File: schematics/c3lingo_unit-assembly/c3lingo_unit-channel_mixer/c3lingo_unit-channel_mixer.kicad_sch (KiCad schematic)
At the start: 93 parts, among them J301 Interconnect, J303 I/O, Q301 MMBFJ113, SW301 OnAir_X, SW302 Mute_X, U301 TL072, U302 LM339, U303 LM339, U304 LM339, U305 LM833-N

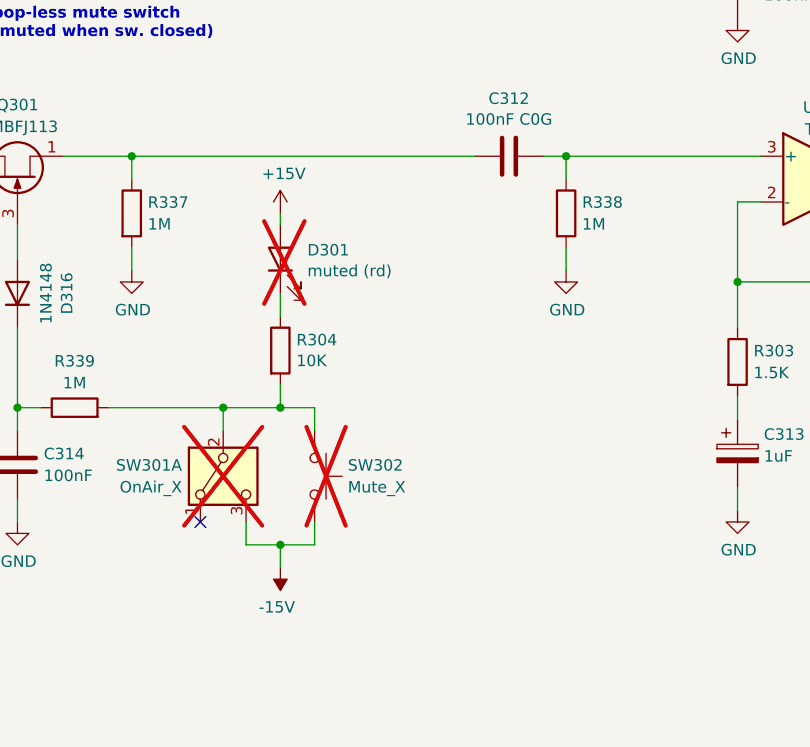
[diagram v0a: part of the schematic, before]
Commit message: Channel-Mixer: Invert mute LED logic (to be an on-air LED)
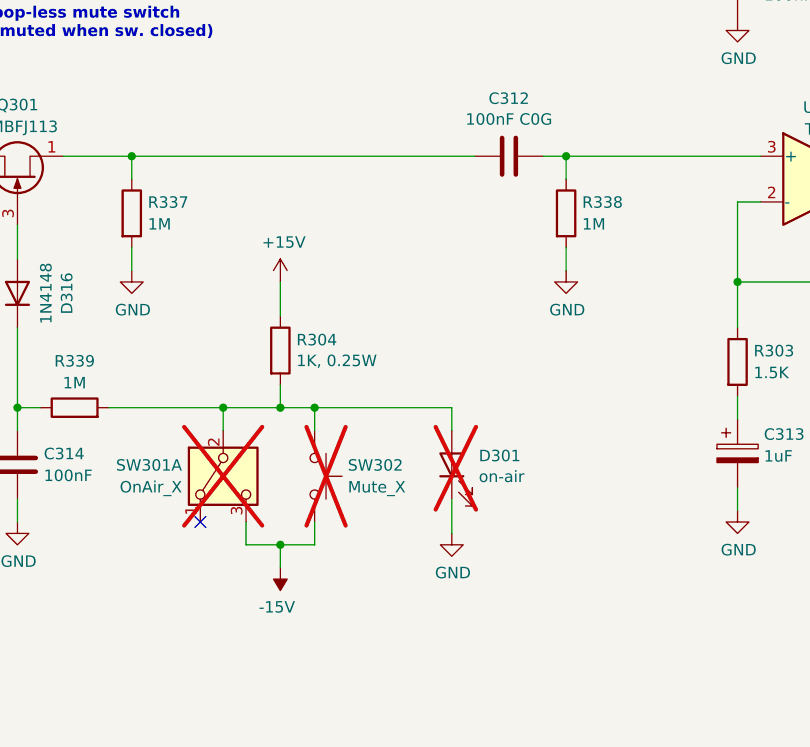
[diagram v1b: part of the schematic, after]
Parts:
- D301: value muted (rd) -> on-air
- R304: value 10K -> 1K, 0.25W; footprint Resistor_SMD:R_0805_2012Metric_Pad1.20x1.40mm_HandSolder -> Resistor_SMD:R_1206_3216Metric_Pad1.30x1.75mm_HandSolder; LCSC Part # C17414 -> C4410
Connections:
- net +15V: now also R304.1; no longer D301.2 (A)
- net GND: now also D301.1 (K)
- net at R304.2, R339.2, SW301.2 (B)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: now also D301.2 (A)
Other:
- moved on the sheet: D301
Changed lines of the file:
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@@
 	)
 	(junction
+		(at 99.06 91.44)
+		(diameter 0)
+		(color 0 0 0 0)
+	)
+	(junction
 		(at 304.8 149.86)
 		(diameter 0)
@@
 	(wire
 		(pts
-			(xy 95.25 78.74) (xy 95.25 81.28)
-		)
-		(stroke
-			(width 0)
-			(type default)
-		)
-	)
-	(wire
-		(pts
 			(xy 229.87 261.62) (xy 229.87 266.7)
 		)
@@
 	(wire
 		(pts
+			(xy 95.25 77.47) (xy 95.25 81.28)
+		)
+		(stroke
+			(width 0)
+			(type default)
+		)
+	)
+	(wire
+		(pts
 			(xy 85.09 213.36) (xy 85.09 215.9)
 		)
@@
 	(wire
 		(pts
-			(xy 95.25 69.85) (xy 95.25 71.12)
-		)
-		(stroke
-			(width 0)
-			(type default)
-		)
-	)
-	(wire
-		(pts
 			(xy 166.37 66.04) (xy 163.83 66.04)
 		)
@@
 	(wire
 		(pts
+			(xy 114.3 91.44) (xy 99.06 91.44)
+		)
+		(stroke
+			(width 0)
+			(type default)
+		)
+	)
+	(wire
+		(pts
 			(xy 304.8 170.18) (xy 304.8 172.72)
 		)
@@
 	(wire
 		(pts
+			(xy 114.3 93.98) (xy 114.3 91.44)
+		)
+		(stroke
+			(width 0)
+			(type default)
+		)
+	)
+	(wire
+		(pts
 			(xy 127 63.5) (xy 148.59 63.5)
 		)
@@
 	(wire
 		(pts
+			(xy 114.3 101.6) (xy 114.3 105.41)
+		)
+		(stroke
+			(width 0)
+			(type default)
+		)
+	)
+	(wire
+		(pts
 			(xy 69.85 215.9) (xy 69.85 218.44)
 		)
@@
 	(symbol
 		(lib_id "Device:LED")
-		(at 95.25 74.93 90)
+		(at 114.3 97.79 90)
 		(unit 1)
 		(exclude_from_sim no)
@@
 		(dnp yes)
 		(property "Reference" "D301"
-			(at 98.2472 73.9394 90)
+			(at 117.2972 96.7994 90)
 			(effects
 				(font
@@
 			)
 		)
-		(property "Value" "muted (rd)"
-			(at 98.2472 76.2508 90)
+		(property "Value" "on-air"
+			(at 117.2972 99.1108 90)
 			(effects
 				(font
@@
 		)
 		(property "Footprint" "LED_THT:LED_D3.0mm"
-			(at 95.25 74.93 0)
+			(at 114.3 97.79 0)
 			(effects
 				(font
@@
 		)
 		(property "Datasheet" "~"
-			(at 95.25 74.93 0)
+			(at 114.3 97.79 0)
 			(effects
 				(font
@@
 		)
 		(property "Description" "Light emitting diode"
-			(at 95.25 74.93 0)
+			(at 114.3 97.79 0)
 			(effects
 				(font
@@
 		)
 		(property "Model" "Kingbright WP710A10LID"
-			(at 95.25 74.93 0)
+			(at 114.3 97.79 0)
 			(effects
 				(font
@@
 		)
 		(property "LCSC Part #" ""
-			(at 95.25 74.93 0)
+			(at 114.3 97.79 0)
 			(effects
 				(font
@@
 		)
 		(property "FT Rotation Offset" ""
-			(at 95.25 74.93 0)
+			(at 114.3 97.79 0)
 			(effects
 				(font
@@
 		)
 		(property "Sim.Pins" "1=K 2=A"
-			(at 95.25 74.93 0)
+			(at 114.3 97.79 0)
 			(effects
 				(font
@@
 			)
 		)
-		(property "Value" "10K"
+		(property "Value" "1K, 0.25W"
 			(at 97.028 86.233 0)
 			(effects
@@
 			)
 		)
-		(property "Footprint" "Resistor_SMD:R_0805_2012Metric_Pad1.20x1.40mm_HandSolder"
+		(property "Footprint" "Resistor_SMD:R_1206_3216Metric_Pad1.30x1.75mm_HandSolder"
 			(at 93.472 85.09 90)
 			(effects
@@
 			)
 		)
-		(property "LCSC Part #" "C17414"
+		(property "LCSC Part #" "C4410"
 			(at 95.25 85.09 0)
 			(effects
@@
 	(symbol
 		(lib_id "power:+15V")
-		(at 95.25 69.85 0)
+		(at 95.25 77.47 0)
 		(unit 1)
 		(exclude_from_sim no)
@@
 		(dnp no)
 		(property "Reference" "#PWR0301"
-			(at 95.25 73.66 0)
+			(at 95.25 81.28 0)
 			(effects
 				(font
@@
 		)
 		(property "Value" "+15V"
-			(at 95.631 65.4558 0)
+			(at 95.631 73.0758 0)
 			(effects
 				(font
@@
 		)
 		(property "Footprint" ""
-			(at 95.25 69.85 0)
+			(at 95.25 77.47 0)
 			(effects
 				(font
@@
 		)
 		(property "Datasheet" ""
-			(at 95.25 69.85 0)
+			(at 95.25 77.47 0)
 			(effects
 				(font
@@
 		)
 		(property "Description" "Power symbol creates a global label with name \"+15V\""
-			(at 95.25 69.85 0)
+			(at 95.25 77.47 0)
 			(effects
 				(font
@@
 					(unit 1)
 				)
+			)
+		)
+	)
+	(symbol
+		(lib_id "power:GND")
+		(at 114.3 105.41 0)
+		(unit 1)
+		(exclude_from_sim no)
+		(in_bom yes)
+		(on_board yes)
+		(dnp no)
+		(property "Reference" "#PWR0333"
+			(at 114.3 111.76 0)
+			(effects
+				(font
+					(size 1.27 1.27)
+				)
+				(hide yes)
+			)
+		)
+		(property "Value" "GND"
+			(at 114.427 109.8042 0)
+			(effects
+				(font
+					(size 1.27 1.27)
+				)
+			)
+		)
+		(property "Footprint" ""
+			(at 114.3 105.41 0)
+			(effects
+				(font
+					(size 1.27 1.27)
+				)
+				(hide yes)
+			)
+		)
+		(property "Datasheet" ""
+			(at 114.3 105.41 0)
+			(effects
+				(font
+					(size 1.27 1.27)
+				)
+				(hide yes)
+			)
+		)
+		(property "Description" "Power symbol creates a global label with name \"GND\" , ground"
+			(at 114.3 105.41 0)
+			(effects
+				(font
+					(size 1.27 1.27)
+				)
+				(hide yes)
+			)
+		)
+		(pin "1"
+		)
+		(instances
+			(project "c3lingo_unit-assembly"
+				(path "/9e80d1ee-62c1-483d-830d-f559e7294d20/00000000-0000-0000-0000-000060aa662f"
+					(reference "#PWR0333")
+					(unit 1)
+				)
+				(path "/9e80d1ee-62c1-483d-830d-f559e7294d20/00000000-0000-0000-0000-000060ae7597"
+					(reference "#PWR0433")
+					(unit 1)
+				)
+				(path "/9e80d1ee-62c1-483d-830d-f559e7294d20/00000000-0000-0000-0000-000060ae80f3"
+					(reference "#PWR0533")
+					(unit 1)
+				)
+			)
+			(project "c3lingo_unit-channel_mixer"
+				(path "/e8e18c84-573e-49d4-a903-1b430b6b9f6d"
+					(reference "#PWR0333")
+					(unit 1)
+				)

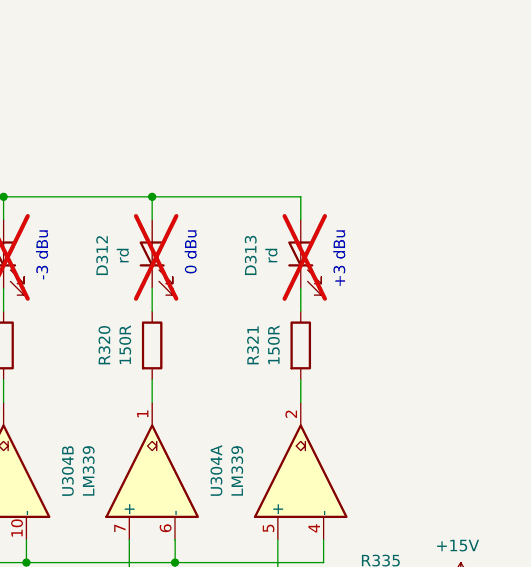
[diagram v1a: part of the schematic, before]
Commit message: Channel-Mixer: Add buffer cap for VU meter LEDs
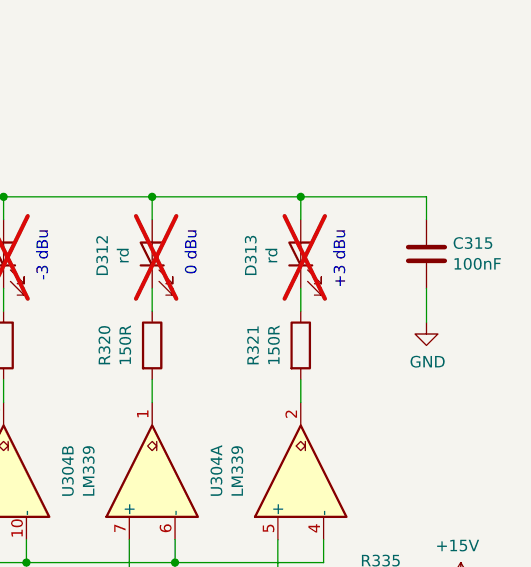
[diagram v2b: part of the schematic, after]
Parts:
- added C315: 100nF, Capacitor_SMD:C_0603_1608Metric_Pad1.08x0.95mm_HandSolder, symbol Device:C
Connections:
- net +5V: now also C315.1
- net GND: now also C315.2
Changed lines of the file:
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@@
 	)
 	(junction
+		(at 337.82 149.86)
+		(diameter 0)
+		(color 0 0 0 0)
+	)
+	(junction
 		(at 158.75 266.7)
 		(diameter 0)
@@
 	(wire
 		(pts
+			(xy 351.79 160.02) (xy 351.79 163.83)
+		)
+		(stroke
+			(width 0)
+			(type default)
+		)
+	)
+	(wire
+		(pts
 			(xy 95.25 88.9) (xy 95.25 91.44)
 		)
@@
 	(wire
 		(pts
+			(xy 351.79 149.86) (xy 351.79 152.4)
+		)
+		(stroke
+			(width 0)
+			(type default)
+		)
+	)
+	(wire
+		(pts
 			(xy 232.41 254) (xy 232.41 251.46)
 		)
@@
 	(wire
 		(pts
+			(xy 337.82 149.86) (xy 351.79 149.86)
+		)
+		(stroke
+			(width 0)
+			(type default)
+		)
+	)
+	(wire
+		(pts
 			(xy 290.83 78.74) (xy 288.29 78.74)
 		)
@@
 	(symbol
 		(lib_id "power:GND")
+		(at 351.79 163.83 0)
+		(unit 1)
+		(exclude_from_sim no)
+		(in_bom yes)
+		(on_board yes)
+		(dnp no)
+		(property "Reference" "#PWR0343"
+			(at 351.79 170.18 0)
+			(effects
+				(font
+					(size 1.27 1.27)
+				)
+				(hide yes)
+			)
+		)
+		(property "Value" "GND"
+			(at 351.917 168.2242 0)
+			(effects
+				(font
+					(size 1.27 1.27)
+				)
+			)
+		)
+		(property "Footprint" ""
+			(at 351.79 163.83 0)
+			(effects
+				(font
+					(size 1.27 1.27)
+				)
+				(hide yes)
+			)
+		)
+		(property "Datasheet" ""
+			(at 351.79 163.83 0)
+			(effects
+				(font
+					(size 1.27 1.27)
+				)
+				(hide yes)
+			)
+		)
+		(property "Description" "Power symbol creates a global label with name \"GND\" , ground"
+			(at 351.79 163.83 0)
+			(effects
+				(font
+					(size 1.27 1.27)
+				)
+				(hide yes)
+			)
+		)
+		(pin "1"
+		)
+		(instances
+			(project "c3lingo_unit-assembly"
+				(path "/9e80d1ee-62c1-483d-830d-f559e7294d20/00000000-0000-0000-0000-000060aa662f"
+					(reference "#PWR0343")
+					(unit 1)
+				)
+				(path "/9e80d1ee-62c1-483d-830d-f559e7294d20/00000000-0000-0000-0000-000060ae7597"
+					(reference "#PWR0443")
+					(unit 1)
+				)
+				(path "/9e80d1ee-62c1-483d-830d-f559e7294d20/00000000-0000-0000-0000-000060ae80f3"
+					(reference "#PWR0543")
+					(unit 1)
+				)
+			)
+			(project "c3lingo_unit-channel_mixer"
+				(path "/e8e18c84-573e-49d4-a903-1b430b6b9f6d"
+					(reference "#PWR0343")
+					(unit 1)
+				)
+			)
+		)
+	)
+	(symbol
+		(lib_id "power:GND")
 		(at 66.04 104.14 0)
 		(unit 1)
@@
 					(unit 1)
 				)
+			)
+		)
+	)
+	(symbol
+		(lib_id "Device:C")
+		(at 351.79 156.21 0)
+		(unit 1)
+		(exclude_from_sim no)
+		(in_bom yes)
+		(on_board yes)
+		(dnp no)
+		(property "Reference" "C315"
+			(at 354.711 155.0416 0)
+			(effects
+				(font
+					(size 1.27 1.27)
+				)
+				(justify left)
+			)
+		)
+		(property "Value" "100nF"
+			(at 354.711 157.353 0)
+			(effects
+				(font
+					(size 1.27 1.27)
+				)
+				(justify left)
+			)
+		)
+		(property "Footprint" "Capacitor_SMD:C_0603_1608Metric_Pad1.08x0.95mm_HandSolder"
+			(at 352.7552 160.02 0)
+			(effects
+				(font
+					(size 1.27 1.27)
+				)
+				(hide yes)
+			)
+		)
+		(property "Datasheet" "~"
+			(at 351.79 156.21 0)
+			(effects
+				(font
+					(size 1.27 1.27)
+				)
+				(hide yes)
+			)
+		)
+		(property "Description" ""
+			(at 351.79 156.21 0)
+			(effects
+				(font
+					(size 1.27 1.27)
+				)
+				(hide yes)
+			)
+		)
+		(property "LCSC Part #" "C14663"
+			(at 351.79 156.21 0)
+			(effects
+				(font
+					(size 1.27 1.27)
+				)
+				(hide yes)
+			)
+		)
+		(property "Model" "10% X7R 25V+"
+			(at 351.79 156.21 0)
+			(effects
+				(font
+					(size 1.27 1.27)
+				)
+				(hide yes)
+			)
+		)
+		(property "FT Rotation Offset" ""
+			(at 351.79 156.21 0)
+			(effects
+				(font
+					(size 1.27 1.27)
+				)
+				(hide yes)
+			)
+		)
+		(pin "1"
+		)
+		(pin "2"
+		)
+		(instances
+			(project "c3lingo_unit-assembly"
+				(path "/9e80d1ee-62c1-483d-830d-f559e7294d20/00000000-0000-0000-0000-000060aa662f"
+					(reference "C315")
+					(unit 1)
+				)
+				(path "/9e80d1ee-62c1-483d-830d-f559e7294d20/00000000-0000-0000-0000-000060ae7597"
+					(reference "C415")
+					(unit 1)
+				)
+				(path "/9e80d1ee-62c1-483d-830d-f559e7294d20/00000000-0000-0000-0000-000060ae80f3"
+					(reference "C515")
+					(unit 1)
+				)
+			)
+			(project "c3lingo_unit-channel_mixer"
+				(path "/e8e18c84-573e-49d4-a903-1b430b6b9f6d"
+					(reference "C315")
+					(unit 1)
+				)

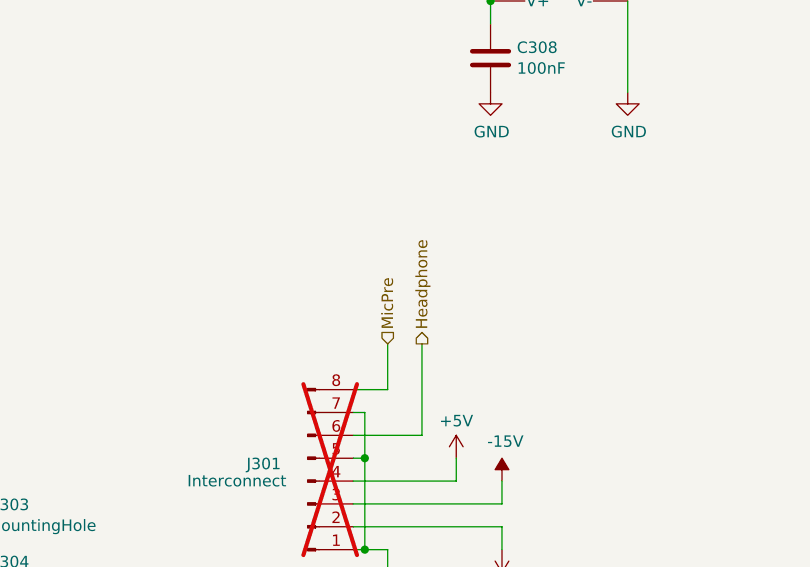
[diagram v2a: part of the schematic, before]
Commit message: Channel: Swap mic and headphone signal on IDC connector
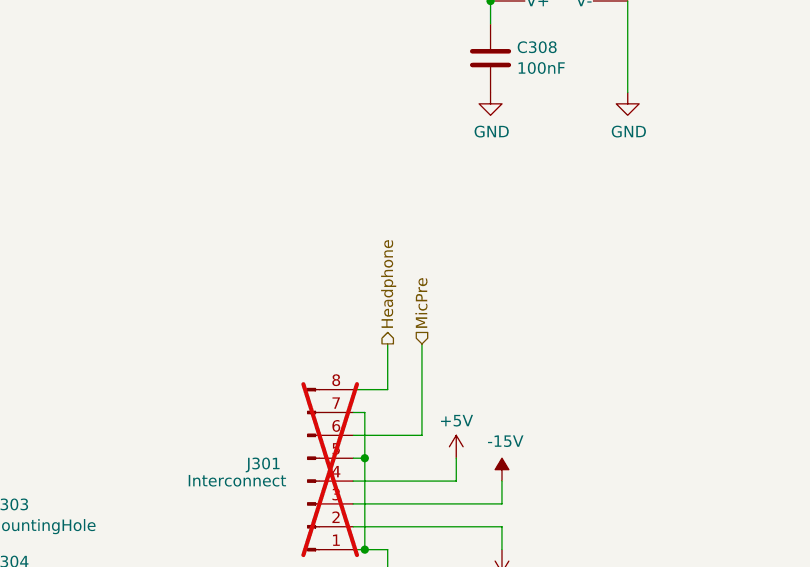
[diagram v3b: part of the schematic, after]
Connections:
- net Headphone: now also J301.8 (Pin_8); no longer J301.6 (Pin_6)
- net MicPre: now also J301.6 (Pin_6); no longer J301.8 (Pin_8)
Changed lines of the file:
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@@
 	(title_block
 		(title "c3lingo interpeter unit -- channel mixer")
-		(date "2025-09-19")
+		(date "2025-09-29")
 		(rev "v0.5.0-dev")
 		(company "Jannik Beyerstedt (jtbx)")
@@
 	(hierarchical_label "MicPre"
 		(shape input)
-		(at 161.29 254 90)
+		(at 165.1 254 90)
 		(effects
 			(font
@@
 	(hierarchical_label "Headphone"
 		(shape output)
-		(at 165.1 254 90)
+		(at 161.29 254 90)
 		(effects
 			(font

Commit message: chore: Bump version number, plot schematic
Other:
- note added: "Errata to v0.4.0: - mute LED logic reworked, is on-air LED now"
- company: Jannik Beyerstedt (jtbx) -> c3lingo/ c3voc: jtbx and collaborators
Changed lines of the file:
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@@
 	(title_block
 		(title "c3lingo interpeter unit -- channel mixer")
-		(date "2025-09-29")
-		(rev "v0.5.0-dev")
-		(company "Jannik Beyerstedt (jtbx)")
-		(comment 1 "Prototype 3b")
+		(date "2025-10-16")
+		(rev "v1.0.0")
+		(company "c3lingo/ c3voc: jtbx and collaborators")
 	)
 	(text "Summing Module\nGain: -inf to 0 dB per Ch."
@@
 		(effects
 			(font
+				(size 1.27 1.27)
+			)
+			(justify left bottom)
+		)
+	)
+	(text "Errata to v0.4.0:\n- mute LED logic reworked, is on-air LED now"
+		(exclude_from_sim no)
+		(at 299.974 250.952 0)
+		(effects
+			(font

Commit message: channel: Select alternate JLCPCB parts
Some capacitors were not in stock any more, so select some other ones
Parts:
- C305, C313: LCSC Part # C336256 -> C445065
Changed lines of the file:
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@@
 			)
 		)
-		(property "LCSC Part #" "C336256"
+		(property "LCSC Part #" "C445065"
 			(at 49.53 187.96 0)
 			(effects
@@
 			)
 		)
-		(property "LCSC Part #" "C336256"
+		(property "LCSC Part #" "C445065"
 			(at 146.05 96.52 0)
 			(effects

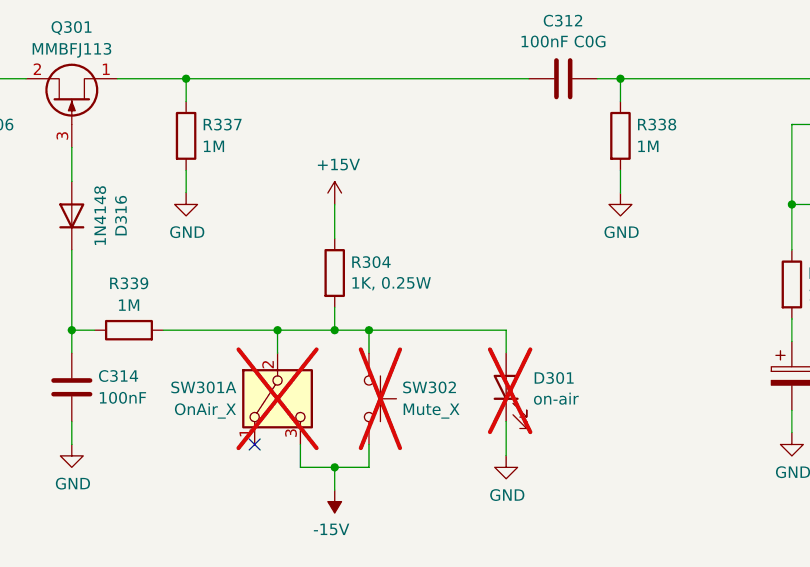
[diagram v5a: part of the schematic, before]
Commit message: Channel-Mixer: Fix on-air LED resistor
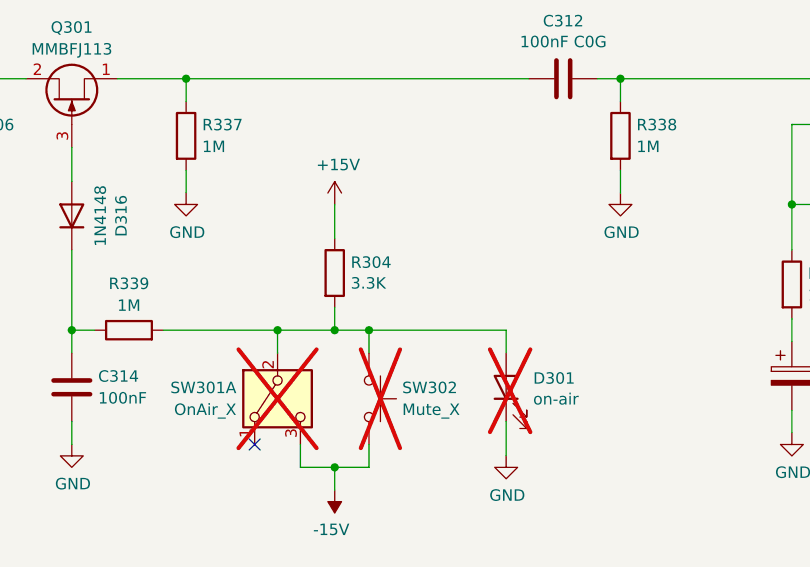
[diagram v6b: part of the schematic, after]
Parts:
- R304: value 1K, 0.25W -> 3.3K; footprint Resistor_SMD:R_1206_3216Metric_Pad1.30x1.75mm_HandSolder -> Resistor_SMD:R_0805_2012Metric_Pad1.20x1.40mm_HandSolder; LCSC Part # C4410 -> C26010
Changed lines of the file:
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@@
 	(title_block
 		(title "c3lingo interpeter unit -- channel mixer")
-		(date "2025-10-16")
-		(rev "v1.0.0")
+		(date "2025-10-29")
+		(rev "v1.0.1")
 		(company "c3lingo/ c3voc: jtbx and collaborators")
 	)
@@
 			)
 		)
-		(property "Value" "1K, 0.25W"
+		(property "Value" "3.3K"
 			(at 97.028 86.233 0)
 			(effects
@@
 			)
 		)
-		(property "Footprint" "Resistor_SMD:R_1206_3216Metric_Pad1.30x1.75mm_HandSolder"
+		(property "Footprint" "Resistor_SMD:R_0805_2012Metric_Pad1.20x1.40mm_HandSolder"
 			(at 93.472 85.09 90)
 			(effects
@@
 			)
 		)
-		(property "LCSC Part #" "C4410"
+		(property "LCSC Part #" "C26010"
 			(at 95.25 85.09 0)
 			(effects
